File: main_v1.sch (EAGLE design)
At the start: 44 parts, among them IC1 MEGA8-P, IC2 7805TV, IC4 MC33063/MC34063P, IC5 MAX6921, IC6 MAX6921

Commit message: Fix some trace widths
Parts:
- R13: device resistor:R-EU_0204/2V -> resistor:R-EU_0207/10
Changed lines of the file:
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@@
 <part name="R11" library="resistor" deviceset="R-EU_" device="0204/7"/>
 <part name="R12" library="resistor" deviceset="R-EU_" device="0204/7"/>
-<part name="R13" library="resistor" deviceset="R-EU_" device="0204/2V"/>
+<part name="R13" library="resistor" deviceset="R-EU_" device="0207/10"/>
 <part name="R14" library="resistor" deviceset="R-EU_" device="0204/7"/>
 <part name="R15" library="resistor" deviceset="R-EU_" device="0204/7" value="4k7"/>

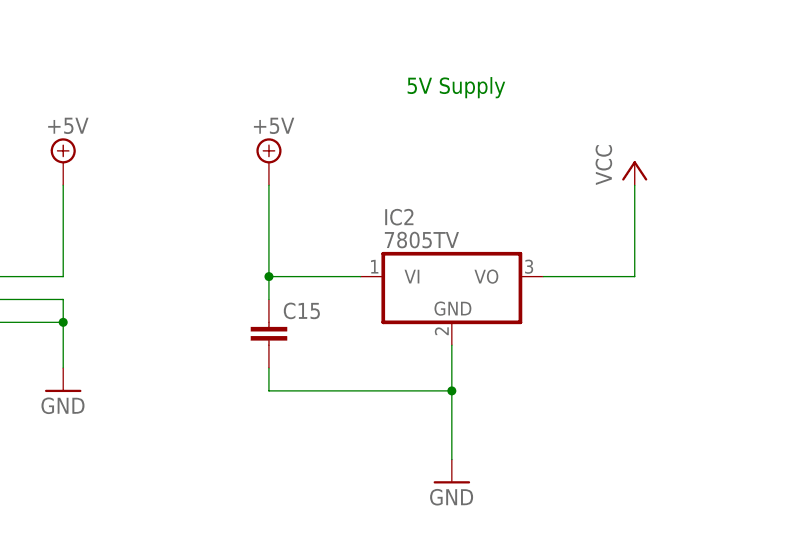
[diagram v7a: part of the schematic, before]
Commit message: Replace LM7805 with LD33v
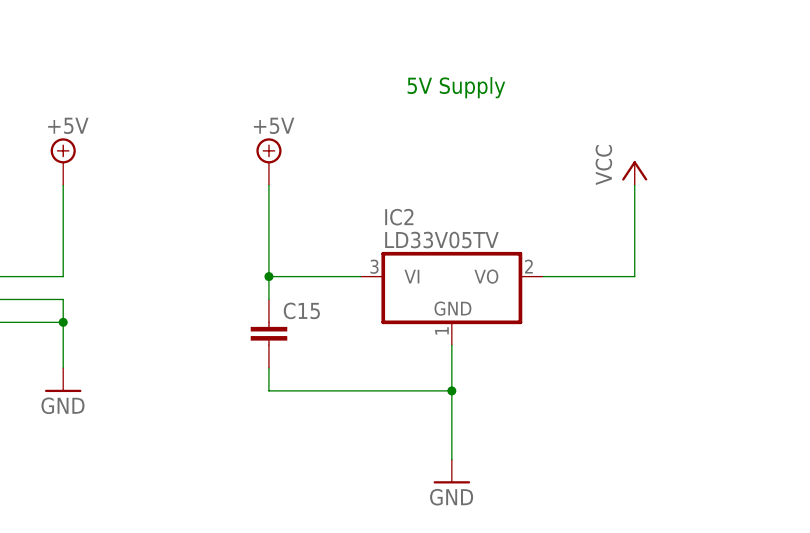
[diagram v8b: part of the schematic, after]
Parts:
- IC2: value 7805TV -> LD33V05TV; device linear:7805TV -> ld33v:LD33V05TV
